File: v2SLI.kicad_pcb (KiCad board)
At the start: 2 copper layers, 77.7 x 75.9 mm, 69 parts, among them J1 Inter-MCU Interrupts Header, J10 Programming Header for 205, J11 Boot 0, J12 Boot 1, J13 Boot 1, J14 Programming Header for 103, J15 Boot 0, J16 SPI Bus, J17 Enable Fix, J18 GPIOs, J19 UART1, J2 Inter-MCU UART Header, J20 Micro_SD_Card, J21 Radio UART, J22 VCC RAIL, J23 GND RAIL, J3 SPI Bus, J4 UART1, J5 205GPIOs, J6 UART2, J7 I2C1, J8 Conn_02x15_Top_Bottom, J9 Conn_02x15_Top_Bottom, SW1 SW_Push, SW2 SW_Push, SW3 SW_Push, U1 STM32F205RETx, U2 BMP388, U3 BMP388, U4 ICM20948, U5 TCR2EE185-SOT553, U6 ADA746, U7 STM32F103C8Tx, U8 Xbee

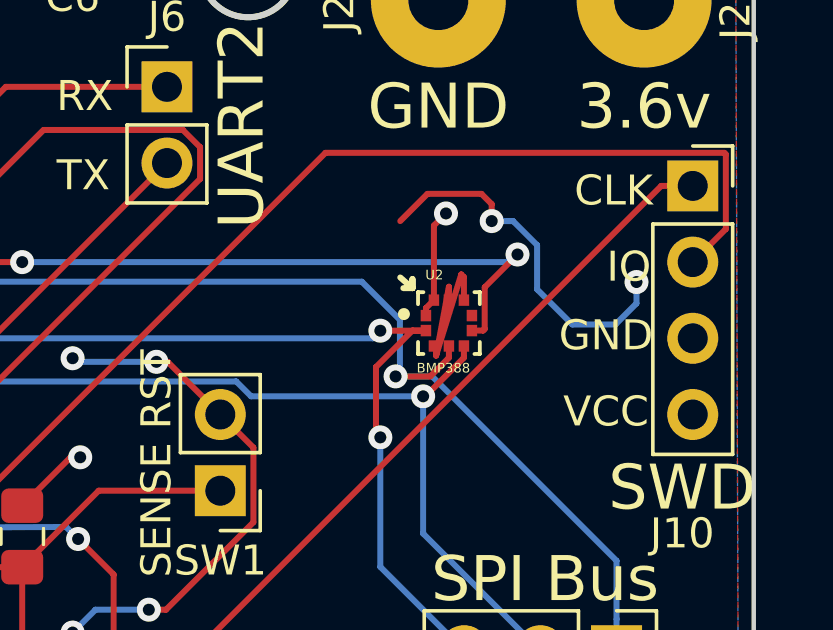
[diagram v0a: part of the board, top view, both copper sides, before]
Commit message: Fixed some shorts that resulted in MOSI being pulled low.
For some reason Kicad didn't enforce the netlist? didn't catch in DRC?
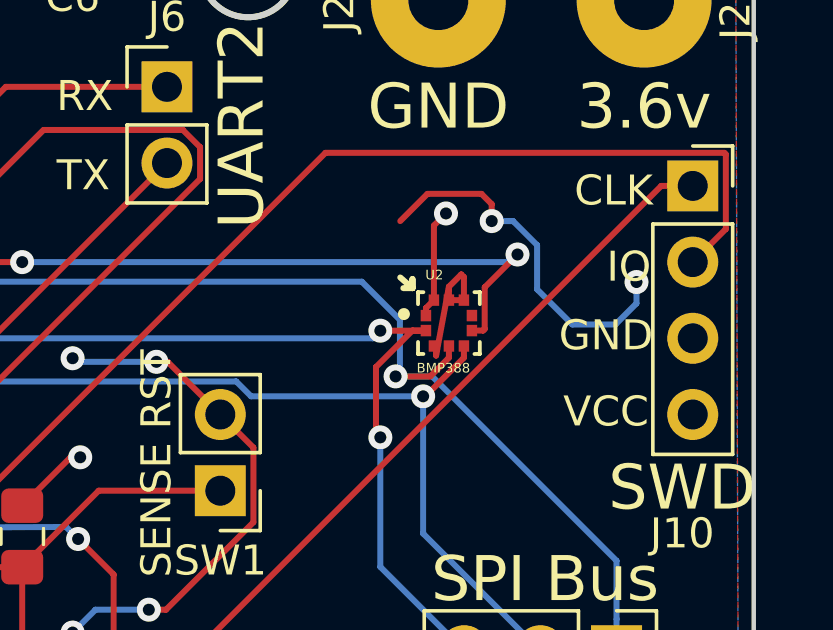
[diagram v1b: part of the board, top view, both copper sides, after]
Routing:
- net GND: track 149.4 -> 147.6 mm
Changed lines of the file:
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@@
     (thickness 1.6)
     (drawings 100)
-    (tracks 1099)
+    (tracks 1100)
     (zones 0)
     (modules 69)
@@
   (segment (start 191.524 48.191001) (end 191.595999 48.191001) (width 0.2) (layer F.Cu) (net 2))
   (segment (start 191.595999 48.581771) (end 192.024 46.286518) (width 0.2) (layer F.Cu) (net 2))
-  (segment (start 192.434259 45.876259) (end 191.595999 48.581771) (width 0.2) (layer F.Cu) (net 2))
   (segment (start 144.518 36.065) (end 144.018 36.065) (width 0.2) (layer F.Cu) (net 2))
   (segment (start 169.521001 61.825001) (end 170.082259 62.386259) (width 0.2) (layer F.Cu) (net 2))
@@
   (segment (start 185.674 104.174) (end 185.727001 104.227001) (width 0.2) (layer F.Cu) (net 2))
   (segment (start 185.674 103.124) (end 185.674 104.174) (width 0.2) (layer F.Cu) (net 2))
+  (segment (start 192.524 46.733) (end 192.024 46.733) (width 0.2) (layer F.Cu) (net 2))
+  (segment (start 192.024 46.286518) (end 192.434259 45.876259) (width 0.2) (layer F.Cu) (net 2))
   (via (at 159.258 47.752) (size 0.8) (drill 0.4) (layers F.Cu B.Cu) (net 3))
   (segment (start 159.36 47.752) (end 159.258 47.752) (width 0.2) (layer F.Cu) (net 3))
